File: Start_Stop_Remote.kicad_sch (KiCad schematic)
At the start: 62 parts, among them J1 AVR-ISP-6, Q1 AO3400A, SW1 SW_DIP_x05, SW2 Push_SW, SW3 Push_SW, SW4 Push_SW, SW6 SW_Push_DPDT, U1 ATmega168PA-AU

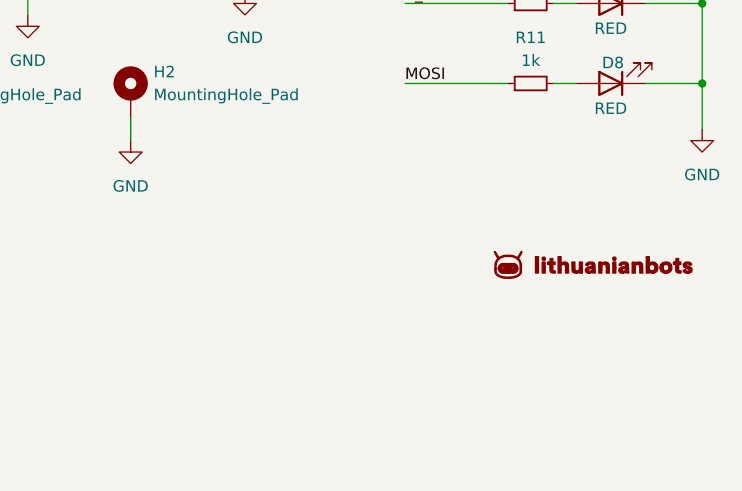
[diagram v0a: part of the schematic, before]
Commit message: QR Code Update
Old QR code was linked to an external website, that has paid service. New one - just links to https://lithuanianbots.com

Library footprint updated as well.
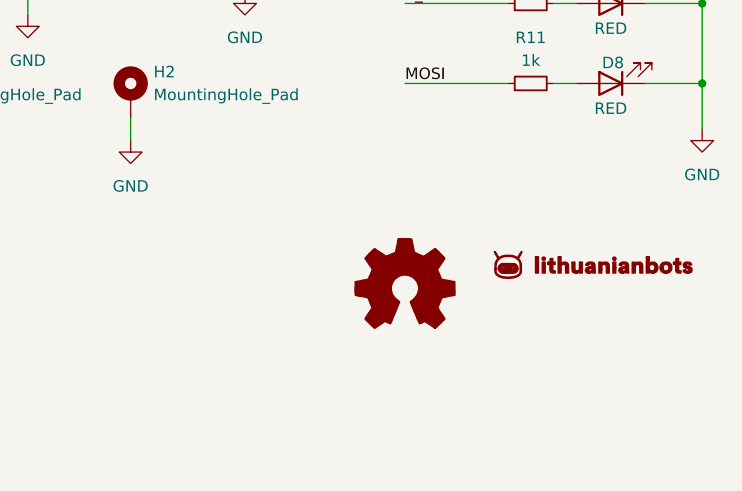
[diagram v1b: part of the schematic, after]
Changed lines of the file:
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@@
+	)
+	(symbol
+		(lib_id "Graphic:Logo_Open_Hardware_Small")
+		(at 247.65 173.99 0)
+		(unit 1)
+		(exclude_from_sim no)
+		(in_bom no)
+		(on_board yes)
+		(dnp no)
+		(fields_autoplaced yes)
+		(property "Reference" "#G2"
+			(at 247.65 167.005 0)
+			(effects
+				(font
+					(size 1.27 1.27)
+				)
+				(hide yes)
+			)
+		)
+		(property "Value" "QR Code symbol"
+			(at 247.65 179.705 0)
+			(effects
+				(font
+					(size 1.27 1.27)
+				)
+				(hide yes)
+			)
+		)
+		(property "Footprint" "_local_lib:LT_Bots_QR_12x12mm"
+			(at 247.65 173.99 0)
+			(effects
+				(font
+					(size 1.27 1.27)
+				)
+				(hide yes)
+			)
+		)
+		(property "Datasheet" "~"
+			(at 247.65 173.99 0)
+			(effects
+				(font
+					(size 1.27 1.27)
+				)
+				(hide yes)
+			)
+		)
+		(property "Description" "QR Code"
+			(at 247.65 173.99 0)
+			(effects
+				(font
+					(size 1.27 1.27)
+				)
+				(hide yes)
+			)
+		)
+		(instances
+			(project ""
+				(path "/67f866dc-324f-452a-b0f3-590d6d136fa3"
+					(reference "#G2")
+					(unit 1)
+				)
+			)
+		)
 	)
 	(symbol
